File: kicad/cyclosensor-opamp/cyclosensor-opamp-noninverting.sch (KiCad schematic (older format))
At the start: 13 parts, among them J1 RJ14

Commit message: changes to mcp6001u circuit - was wrong package!
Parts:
- removed U?: MCP6001, symbol MCP6001
- added GAIN?: 100K, ~, symbol POT
- added R?: 10k, ~, symbol R
- added U?: MCP6001U, ~, symbol MCP6001U
- GAIN1: value 1M -> 100K
- gave numbers to parts that had none: 7
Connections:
- net 5V: now also GAIN?.1, U?.5 (V+)
- net ADC: now also U?.4 (Vout)
- net GND: now also GAIN?.3, U?.2 (V-)
- net at R1.1, U1.3 (Emitter-): now also R?.2, U?.1 (+)
- net at GAIN1.1, R3.1: now also U?.3 (-)
- new net: GAIN?.2, R?.1
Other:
- note added: "Extra stuff for positive\noffset from zero!"
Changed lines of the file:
@@
 EESchema Schematic File Version 2
-LIBS:power
-LIBS:device
-LIBS:transistors
-LIBS:conn
-LIBS:linear
-LIBS:regul
-LIBS:74xx
-LIBS:cmos4000
-LIBS:adc-dac
-LIBS:memory
-LIBS:xilinx
-LIBS:special
-LIBS:microcontrollers
-LIBS:dsp
-LIBS:microchip
-LIBS:analog_switches
-LIBS:motorola
-LIBS:texas
-LIBS:intel
-LIBS:audio
-LIBS:interface
-LIBS:digital-audio
-LIBS:philips
-LIBS:display
-LIBS:cypress
-LIBS:siliconi
-LIBS:opto
-LIBS:atmel
-LIBS:contrib
-LIBS:valves
 LIBS:cyclophone
-LIBS:cyclosensor-opamp-cache
-EELAYER 24 0
+LIBS:cyclosensor-opamp-noninverting-cache
+EELAYER 27 0
 EELAYER END
 $Descr A4 11693 8268
@@
 Sheet 1 1
 Title ""
-Date "16 apr 2014"
+Date "23 apr 2014"
 Rev ""
 Comp ""
@@
 ADC
 $Comp
-L GND #PWR01
+L GND #PWR10
 U 1 1 533B827E
 P 7150 3800
-F 0 "#PWR01" H 7150 3800 30  0001 C CNN
+F 0 "#PWR10" H 7150 3800 30  0001 C CNN
 F 1 "GND" H 7150 3730 30  0001 C CNN
 F 2 "" H 7150 3800 60  0000 C CNN
@@
 5V
 $Comp
-L GND #PWR02
+L GND #PWR6
 U 1 1 533B8353
 P 4900 3950
-F 0 "#PWR02" H 4900 3950 30  0001 C CNN
+F 0 "#PWR6" H 4900 3950 30  0001 C CNN
 F 1 "GND" H 4900 3880 30  0001 C CNN
 F 2 "" H 4900 3950 60  0000 C CNN
@@
 5V
 $Comp
-L GND #PWR05
+L GND #PWR2
 U 1 1 533B9F2F
 P 3650 4400
-F 0 "#PWR05" H 3650 4400 30  0001 C CNN
+F 0 "#PWR2" H 3650 4400 30  0001 C CNN
 F 1 "GND" H 3650 4330 30  0001 C CNN
 F 2 "" H 3650 4400 60  0000 C CNN
@@
 P 4900 3450
 F 0 "GAIN1" H 4900 3350 50  0000 C CNN
-F 1 "1M" H 4900 3450 50  0000 C CNN
+F 1 "100K" H 4900 3450 50  0000 C CNN
 F 2 "~" H 4900 3450 60  0000 C CNN
 F 3 "~" H 4900 3450 60  0000 C CNN
@@
 1M ok for tuning, not too sensitive?
 $Comp
-L C C?
+L C C1
 U 1 1 53449FBF
 P 6450 5250
-F 0 "C?" H 6450 5350 40  0000 L CNN
+F 0 "C1" H 6450 5350 40  0000 L CNN
 F 1 ".01uf" H 6456 5165 40  0000 L CNN
 F 2 "~" H 6488 5100 30  0000 C CNN
@@
 5V
 $Comp
-L GND #PWR?
+L GND #PWR8
 U 1 1 53449FDD
 P 6450 5550
-F 0 "#PWR?" H 6450 5550 30  0001 C CNN
+F 0 "#PWR8" H 6450 5550 30  0001 C CNN
 F 1 "GND" H 6450 5480 30  0001 C CNN
 F 2 "" H 6450 5550 60  0000 C CNN
@@
 Put near pin 8 on op-amp!
 $Comp
-L C C?
+L C C2
 U 1 1 5344A0AE
 P 6800 5250
-F 0 "C?" H 6800 5350 40  0000 L CNN
+F 0 "C2" H 6800 5350 40  0000 L CNN
 F 1 "10uf" H 6806 5165 40  0000 L CNN
 F 2 "~" H 6838 5100 30  0000 C CNN
@@
 5V
 $Comp
-L GND #PWR?
+L GND #PWR9
 U 1 1 5344A0B5
 P 6800 5550
-F 0 "#PWR?" H 6800 5550 30  0001 C CNN
+F 0 "#PWR9" H 6800 5550 30  0001 C CNN
 F 1 "GND" H 6800 5480 30  0001 C CNN
 F 2 "" H 6800 5550 60  0000 C CNN
@@
 option of two caps \nfor different freq\nfiltering on each
 $Comp
-L TCRT5000 U?
+L TCRT5000 U1
 U 1 1 53499E1E
 P 3050 4250
-F 0 "U?" H 3050 3700 60  0000 C CNN
+F 0 "U1" H 3050 3700 60  0000 C CNN
 F 1 "TCRT5000" H 3050 4700 60  0000 C CNN
 F 2 "~" H 3050 4250 60  0000 C CNN
@@
 	4900 3300 5500 3300
 $Comp
-L R R?
+L R R2
 U 1 1 5349C83F
 P 4150 2100
-F 0 "R?" V 4230 2100 40  0000 C CNN
+F 0 "R2" V 4230 2100 40  0000 C CNN
 F 1 "20k" V 4157 2101 40  0000 C CNN
 F 2 "~" V 4080 2100 30  0000 C CNN
@@
 $EndComp
 $Comp
-L GND #PWR?
+L GND #PWR5
 U 1 1 5349C845
 P 4150 2500
-F 0 "#PWR?" H 4150 2500 30  0001 C CNN
+F 0 "#PWR5" H 4150 2500 30  0001 C CNN
 F 1 "GND" H 4150 2430 30  0001 C CNN
 F 2 "" H 4150 2500 60  0000 C CNN
@@
 $EndComp
 $Comp
-L POT OFFSET?
+L POT OFFSET2
 U 1 1 5349C84B
 P 3800 2100
-F 0 "OFFSET?" H 3800 2000 50  0000 C CNN
+F 0 "OFFSET2" H 3800 2000 50  0000 C CNN
 F 1 "20K" H 3800 2100 50  0000 C CNN
 F 2 "~" H 3800 2100 60  0000 C CNN
@@
 	3950 2100 3950 2400
 $Comp
-L GND #PWR?
+L GND #PWR1
 U 1 1 5349C88D
 P 2550 2150
-F 0 "#PWR?" H 2550 2150 30  0001 C CNN
+F 0 "#PWR1" H 2550 2150 30  0001 C CNN
 F 1 "GND" H 2550 2080 30  0001 C CNN
 F 2 "" H 2550 2150 60  0000 C CNN
@@
 	2550 1950 2550 2150
 $Comp
-L GND #PWR?
+L GND #PWR7
 U 1 1 5355C365
 P 5500 5200
-F 0 "#PWR?" H 5500 5200 30  0001 C CNN
+F 0 "#PWR7" H 5500 5200 30  0001 C CNN
 F 1 "GND" H 5500 5130 30  0001 C CNN
 F 2 "" H 5500 5200 60  0000 C CNN
@@
 Connection ~ 5500 4450
 $Comp
-L R R?
+L R R3
 U 1 1 5355C3FF
 P 4150 4350
-F 0 "R?" V 4230 4350 40  0000 C CNN
+F 0 "R3" V 4230 4350 40  0000 C CNN
 F 1 "10k" V 4157 4351 40  0000 C CNN
 F 2 "" V 4080 4350 30  0000 C CNN
@@
 	3650 4300 3650 4400
 $Comp
-L GND #PWR?
+L GND #PWR3
 U 1 1 5355C5B1
 P 3650 5350
-F 0 "#PWR?" H 3650 5350 30  0001 C CNN
+F 0 "#PWR3" H 3650 5350 30  0001 C CNN
 F 1 "GND" H 3650 5280 30  0001 C CNN
 F 2 "" H 3650 5350 60  0000 C CNN
@@
 $EndComp
 $Comp
-L R R?
+L R R4
 U 1 1 5355C5BE
 P 5500 4850
-F 0 "R?" V 5580 4850 40  0000 C CNN
+F 0 "R4" V 5580 4850 40  0000 C CNN
 F 1 "240" V 5507 4851 40  0000 C CNN
 F 2 "" V 5430 4850 30  0000 C CNN
@@
 	5500 5100 5500 5200
 $Comp
-L MCP6001 U?
-U 1 1 5355C33C
-P 5000 4450
-F 0 "U?" H 4950 4650 60  0000 L CNN
-F 1 "MCP6001" H 4950 4200 60  0000 L CNN
-F 2 "" H 5000 4450 60  0000 C CNN
-F 3 "" H 5000 4450 60  0000 C CNN
-	1    5000 4450
-	1    0    0    1
-$EndComp
-$Comp
-L GND #PWR?
+L GND #PWR4
 U 1 1 5355C66A
 P 3850 4400
-F 0 "#PWR?" H 3850 4400 30  0001 C CNN
+F 0 "#PWR4" H 3850 4400 30  0001 C CNN
 F 1 "GND" H 3850 4330 30  0001 C CNN
 F 2 "" H 3850 4400 60  0000 C CNN
@@
 Wire Wire Line
 	3850 4350 3900 4350
+$Comp
+L R R?
+U 1 1 535734BD
+P 3150 5100
+F 0 "R?" V 3230 5100 40  0000 C CNN
+F 1 "10k" V 3157 5101 40  0000 C CNN
+F 2 "~" V 3080 5100 30  0000 C CNN
+F 3 "~" H 3150 5100 30  0000 C CNN
+	1    3150 5100
+	0    -1   -1   0
+$EndComp
+Wire Wire Line
+	3650 4600 3450 4600
+Wire Wire Line
+	3450 4600 3450 5100
+Wire Wire Line
+	3450 5100 3400 5100
+Connection ~ 3650 4600
+$Comp
+L POT GAIN?
+U 1 1 53573527
+P 2750 5100
+F 0 "GAIN?" H 2750 5000 50  0000 C CNN
+F 1 "100K" H 2750 5100 50  0000 C CNN
+F 2 "~" H 2750 5100 60  0000 C CNN
+F 3 "~" H 2750 5100 60  0000 C CNN
+	1    2750 5100
+	0    1    1    0
+$EndComp
+Text GLabel 2750 4850 1    60   Input ~ 0
+5V
+Wire Wire Line
+	2750 5350 2750 5500
+$Comp
+L GND #PWR?
+U 1 1 5357352F
+P 2750 5500
+F 0 "#PWR?" H 2750 5500 30  0001 C CNN
+F 1 "GND" H 2750 5430 30  0001 C CNN
+F 2 "" H 2750 5500 60  0000 C CNN
+F 3 "" H 2750 5500 60  0000 C CNN
+	1    2750 5500
+	1    0    0    -1
+$EndComp
+Text Notes 2300 5700 0    60   ~ 0
+Extra stuff for positive\noffset from zero!
+$Comp
+L MCP6001U U?
+U 1 1 5358437A
+P 5000 4450
+F 0 "U?" H 4950 4650 60  0000 L CNN
+F 1 "MCP6001U" H 4950 4200 60  0000 L CNN
+F 2 "~" H 5000 4450 60  0000 C CNN
+F 3 "~" H 5000 4450 60  0000 C CNN
+	1    5000 4450
+	1    0    0    1
+$EndComp
 $EndSCHEMATC

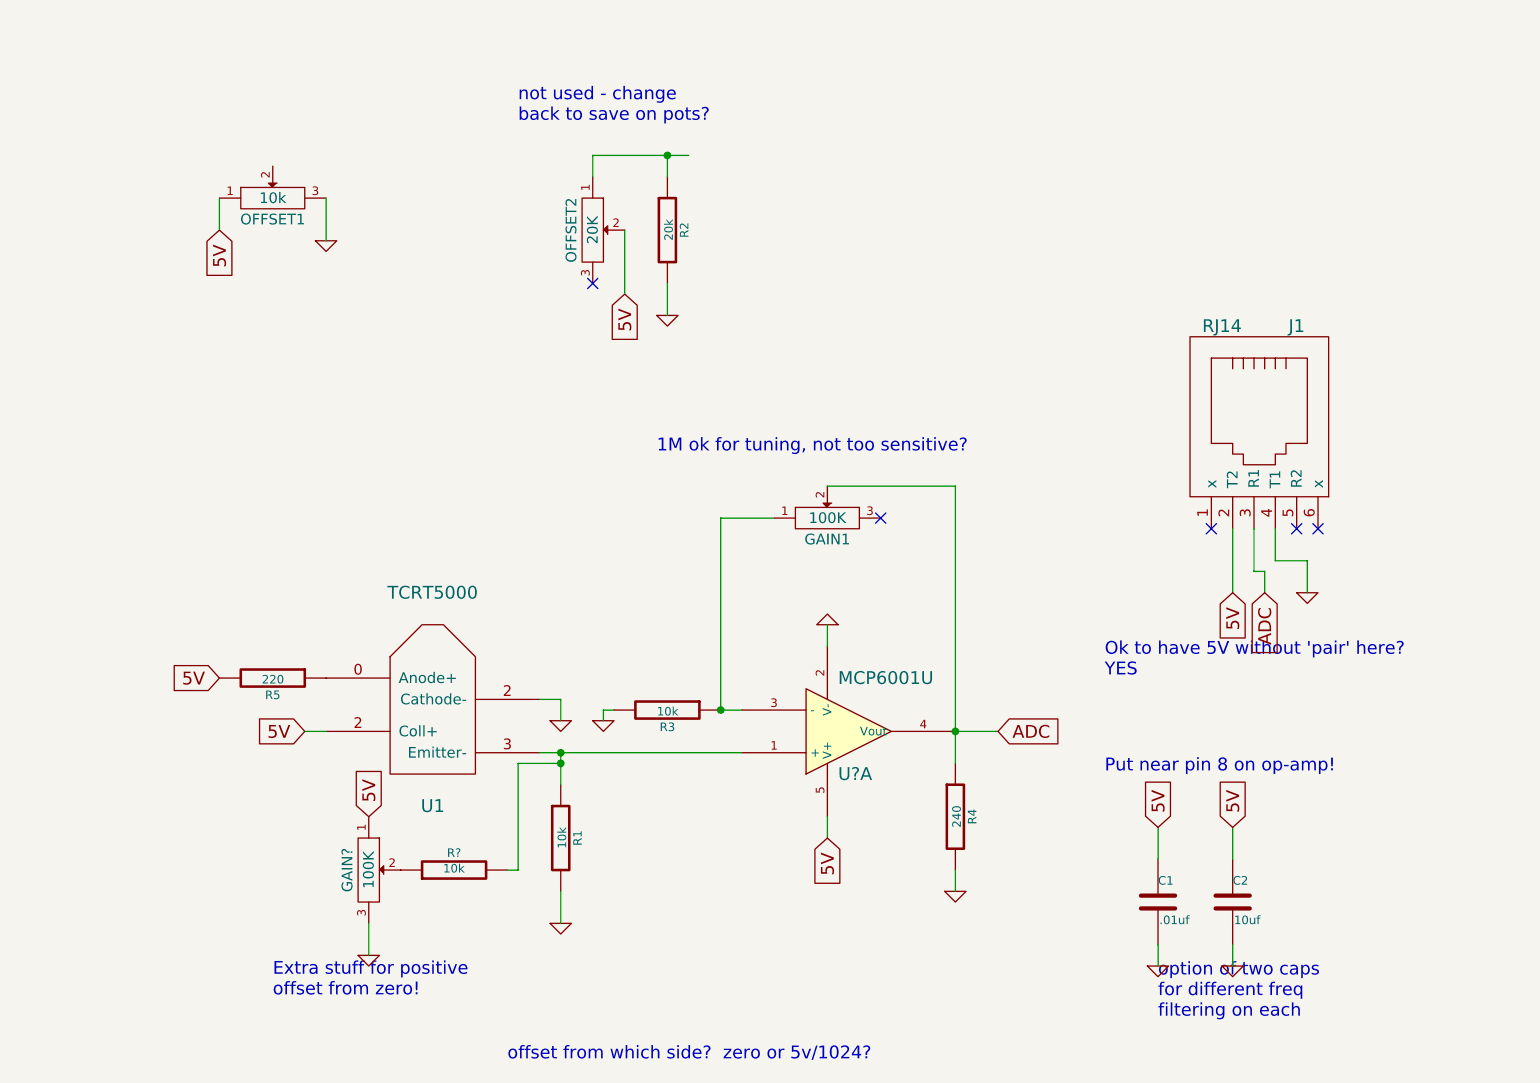
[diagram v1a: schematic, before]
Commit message: tweak opamp circuit to match reality.  added dual opamp circuit for low/high adjustments to sensor range.
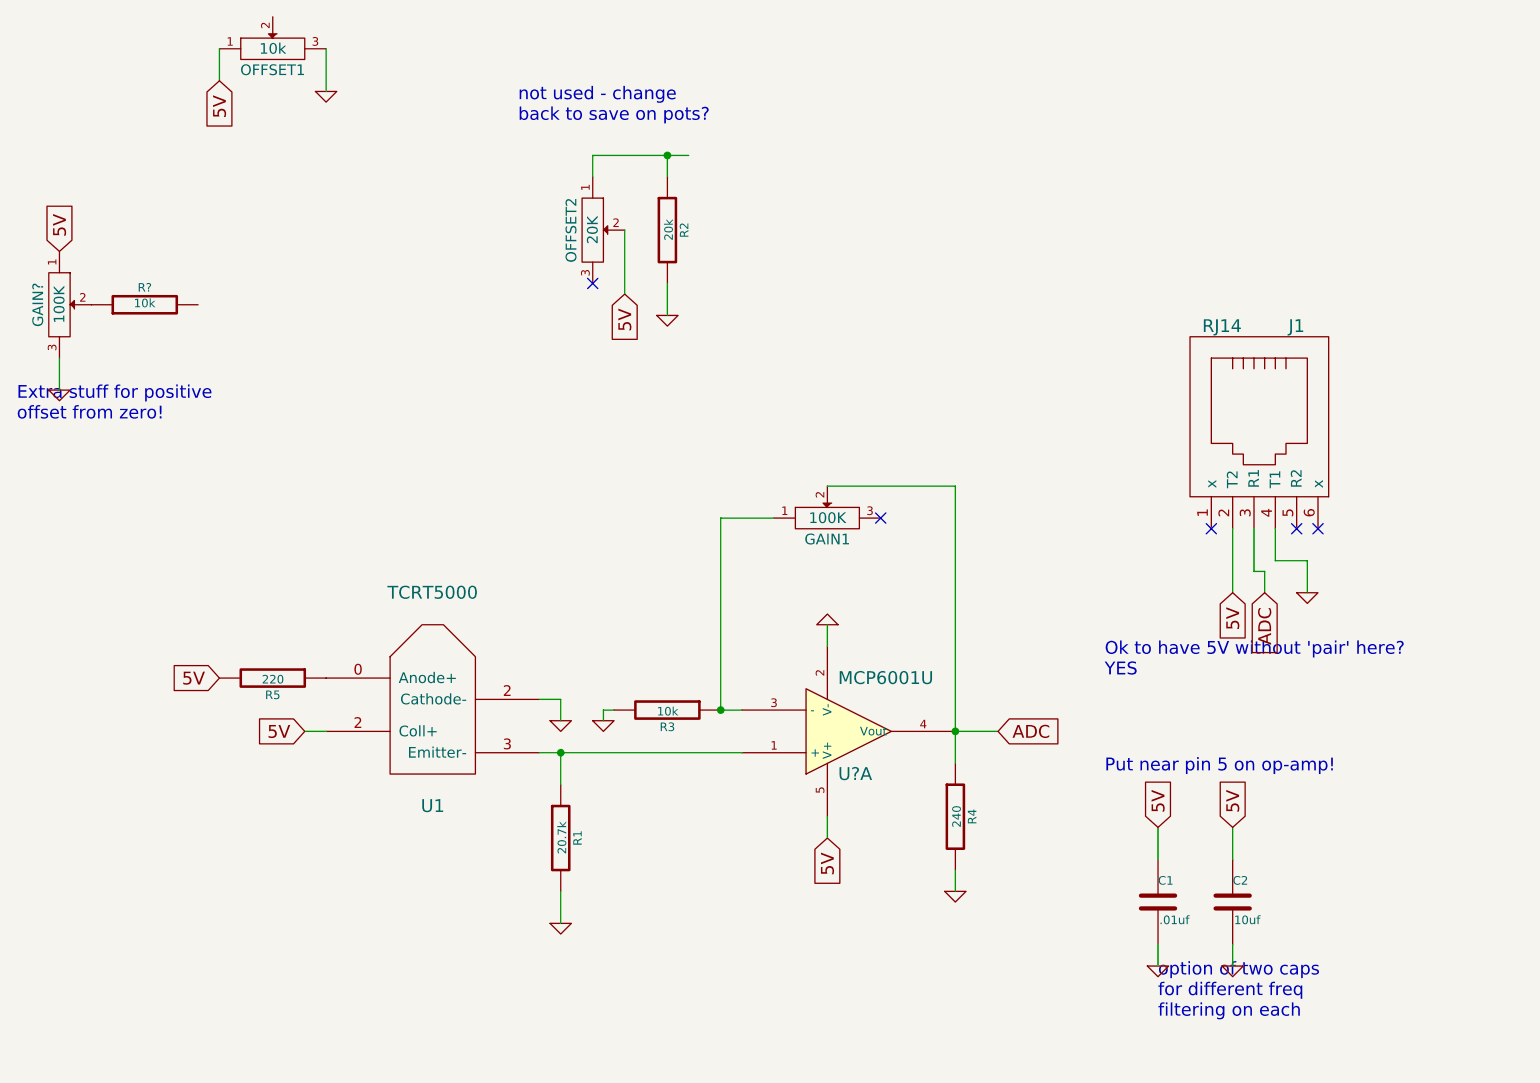
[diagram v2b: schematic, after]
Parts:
- R1: value 10k -> 20.7k
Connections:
- net at R1.1, U1.3 (Emitter-), U?.1 (+): no longer R?.2
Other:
- note added: "Put near pin 5 on op-amp!"
- note removed: "1M ok for tuning, not too sensitive?"
- note removed: "Put near pin 8 on op-amp!"
- note removed: "offset from which side? zero or 5v/1024?"
- moved on the sheet: GAIN?, OFFSET1, R?
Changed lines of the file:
@@
 Sheet 1 1
 Title ""
-Date "23 apr 2014"
+Date "25 apr 2014"
 Rev ""
 Comp ""
@@
 P 3650 4950
 F 0 "R1" V 3730 4950 40  0000 C CNN
-F 1 "10k" V 3657 4951 40  0000 C CNN
+F 1 "20.7k" V 3657 4951 40  0000 C CNN
 F 2 "~" V 3580 4950 30  0000 C CNN
 F 3 "~" H 3650 4950 30  0000 C CNN
@@
 L POT OFFSET1
 U 1 1 533BA12C
-P 2300 1950
-F 0 "OFFSET1" H 2300 1850 50  0000 C CNN
-F 1 "10k" H 2300 1950 50  0000 C CNN
-F 2 "~" H 2300 1950 60  0000 C CNN
-F 3 "~" H 2300 1950 60  0000 C CNN
-	1    2300 1950
-	1    0    0    -1
-$EndComp
-Text GLabel 2050 2100 3    60   Input ~ 0
+P 2300 1250
+F 0 "OFFSET1" H 2300 1150 50  0000 C CNN
+F 1 "10k" H 2300 1250 50  0000 C CNN
+F 2 "~" H 2300 1250 60  0000 C CNN
+F 3 "~" H 2300 1250 60  0000 C CNN
+	1    2300 1250
+	1    0    0    -1
+$EndComp
+Text GLabel 2050 1400 3    60   Input ~ 0
 5V
 NoConn ~ 7100 3500
 Text Notes 6200 4200 0    60   ~ 0
 Ok to have 5V without 'pair' here?  \nYES
-Text Notes 3400 6000 0    60   ~ 0
-offset from which side?  zero or 5v/1024?
-Text Notes 4100 3150 0    60   ~ 0
-1M ok for tuning, not too sensitive?
 $Comp
 L C C1
@@
 $EndComp
 Text Notes 6200 4650 0    60   ~ 0
-Put near pin 8 on op-amp!
+Put near pin 5 on op-amp!
 $Comp
 L C C2
@@
 L GND #PWR1
 U 1 1 5349C88D
-P 2550 2150
-F 0 "#PWR1" H 2550 2150 30  0001 C CNN
-F 1 "GND" H 2550 2080 30  0001 C CNN
-F 2 "" H 2550 2150 60  0000 C CNN
-F 3 "" H 2550 2150 60  0000 C CNN
-	1    2550 2150
-	1    0    0    -1
-$EndComp
-Wire Wire Line
-	2050 2100 2050 1950
+P 2550 1450
+F 0 "#PWR1" H 2550 1450 30  0001 C CNN
+F 1 "GND" H 2550 1380 30  0001 C CNN
+F 2 "" H 2550 1450 60  0000 C CNN
+F 3 "" H 2550 1450 60  0000 C CNN
+	1    2550 1450
+	1    0    0    -1
+$EndComp
+Wire Wire Line
+	2050 1400 2050 1250
 Text Notes 3450 1600 0    60   ~ 0
 not used - change\nback to save on pots?
 Wire Wire Line
-	2550 1950 2550 2150
+	2550 1250 2550 1450
 $Comp
 L GND #PWR7
@@
 L R R?
 U 1 1 535734BD
-P 3150 5100
-F 0 "R?" V 3230 5100 40  0000 C CNN
-F 1 "10k" V 3157 5101 40  0000 C CNN
-F 2 "~" V 3080 5100 30  0000 C CNN
-F 3 "~" H 3150 5100 30  0000 C CNN
-	1    3150 5100
+P 1700 2450
+F 0 "R?" V 1780 2450 40  0000 C CNN
+F 1 "10k" V 1707 2451 40  0000 C CNN
+F 2 "~" V 1630 2450 30  0000 C CNN
+F 3 "~" H 1700 2450 30  0000 C CNN
+	1    1700 2450
 	0    -1   -1   0
 $EndComp
-Wire Wire Line
-	3650 4600 3450 4600
-Wire Wire Line
-	3450 4600 3450 5100
-Wire Wire Line
-	3450 5100 3400 5100
-Connection ~ 3650 4600
 $Comp
 L POT GAIN?
 U 1 1 53573527
-P 2750 5100
-F 0 "GAIN?" H 2750 5000 50  0000 C CNN
-F 1 "100K" H 2750 5100 50  0000 C CNN
-F 2 "~" H 2750 5100 60  0000 C CNN
-F 3 "~" H 2750 5100 60  0000 C CNN
-	1    2750 5100
+P 1300 2450
+F 0 "GAIN?" H 1300 2350 50  0000 C CNN
+F 1 "100K" H 1300 2450 50  0000 C CNN
+F 2 "~" H 1300 2450 60  0000 C CNN
+F 3 "~" H 1300 2450 60  0000 C CNN
+	1    1300 2450
 	0    1    1    0
 $EndComp
-Text GLabel 2750 4850 1    60   Input ~ 0
-5V
-Wire Wire Line
-	2750 5350 2750 5500
+Text GLabel 1300 2200 1    60   Input ~ 0
+5V
+Wire Wire Line
+	1300 2700 1300 2850
 $Comp
 L GND #PWR?
 U 1 1 5357352F
-P 2750 5500
-F 0 "#PWR?" H 2750 5500 30  0001 C CNN
-F 1 "GND" H 2750 5430 30  0001 C CNN
-F 2 "" H 2750 5500 60  0000 C CNN
-F 3 "" H 2750 5500 60  0000 C CNN
-	1    2750 5500
-	1    0    0    -1
-$EndComp
-Text Notes 2300 5700 0    60   ~ 0
+P 1300 2850
+F 0 "#PWR?" H 1300 2850 30  0001 C CNN
+F 1 "GND" H 1300 2780 30  0001 C CNN
+F 2 "" H 1300 2850 60  0000 C CNN
+F 3 "" H 1300 2850 60  0000 C CNN
+	1    1300 2850
+	1    0    0    -1
+$EndComp
+Text Notes 1100 3000 0    60   ~ 0
 Extra stuff for positive\noffset from zero!
 $Comp
